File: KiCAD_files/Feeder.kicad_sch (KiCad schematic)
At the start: 82 parts, among them J405 Conn_01x02_Male, J406 Conn_01x02_Male, J501 Conn_01x03, Q501 60V N channel, Q502 TK13P25D,RQ, T501 PA2467NL, U407 OPA316, U501 NCP12700, U502 FODM217A, U503 TL431MFDT,215

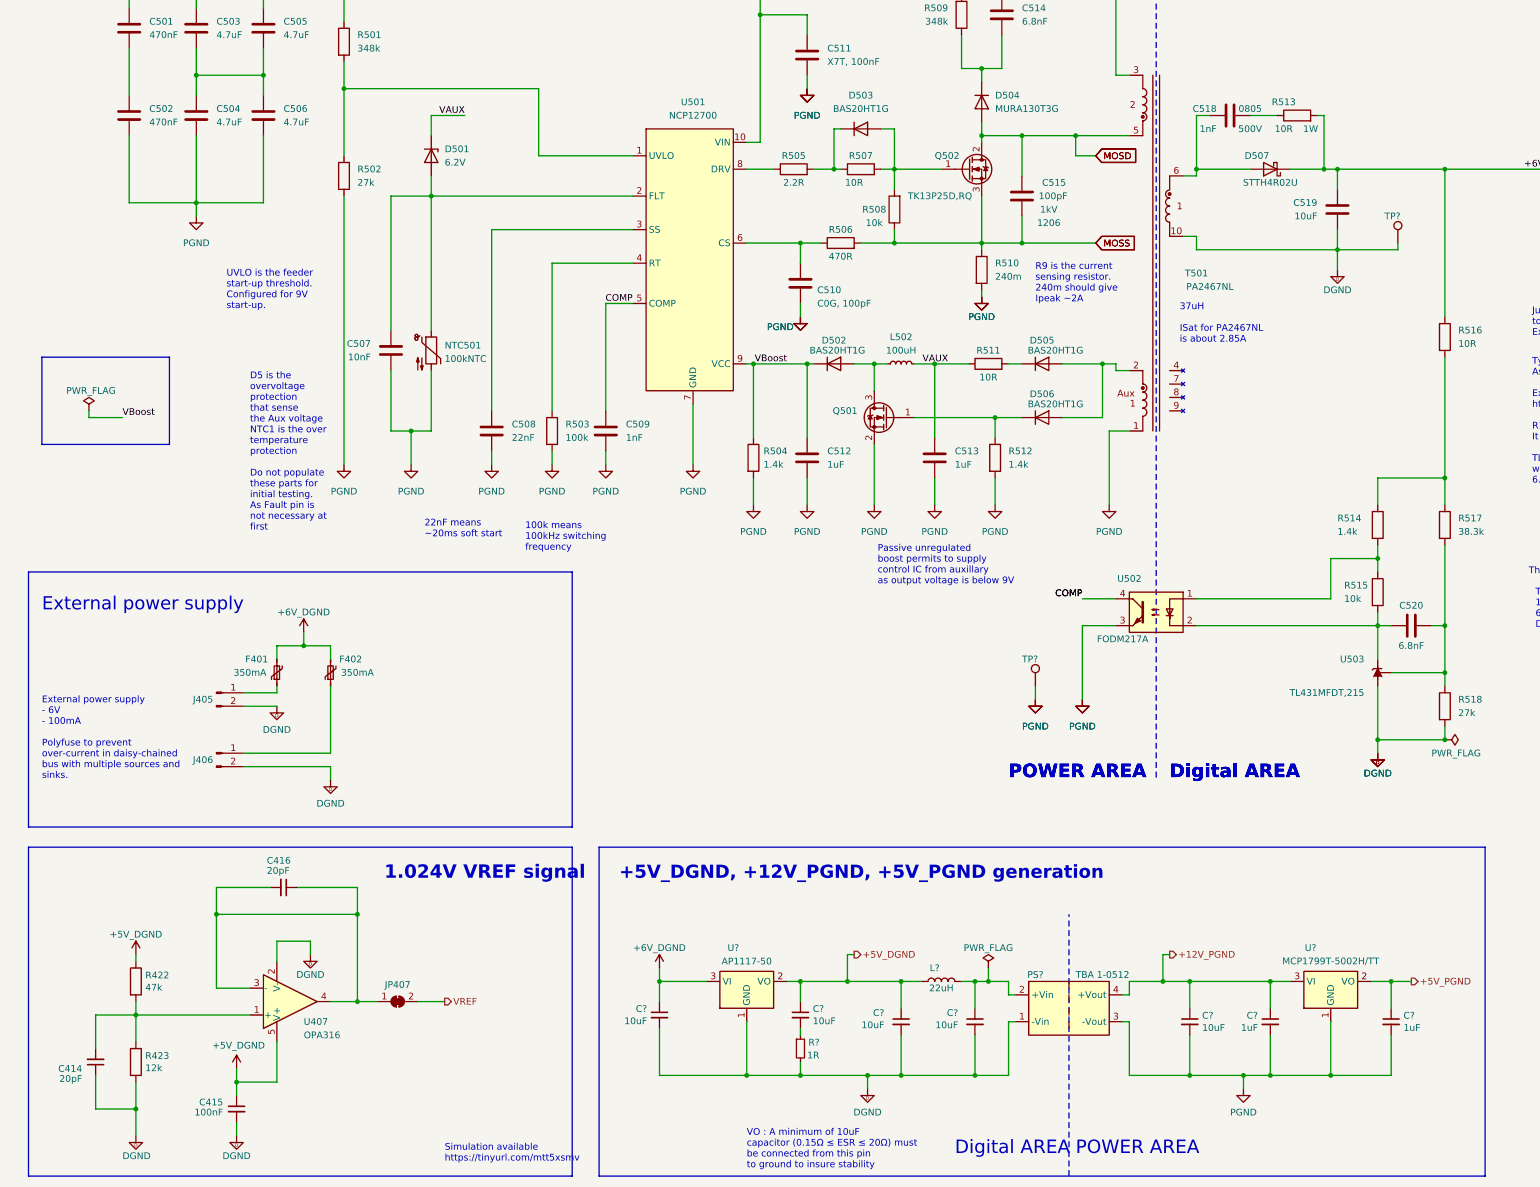
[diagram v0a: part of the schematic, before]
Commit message: Added ERC rules for galvanic isolation. Modified SPIN pinout.
Signed-off-by: Jean Alinei <jean.alinei@laas.fr>
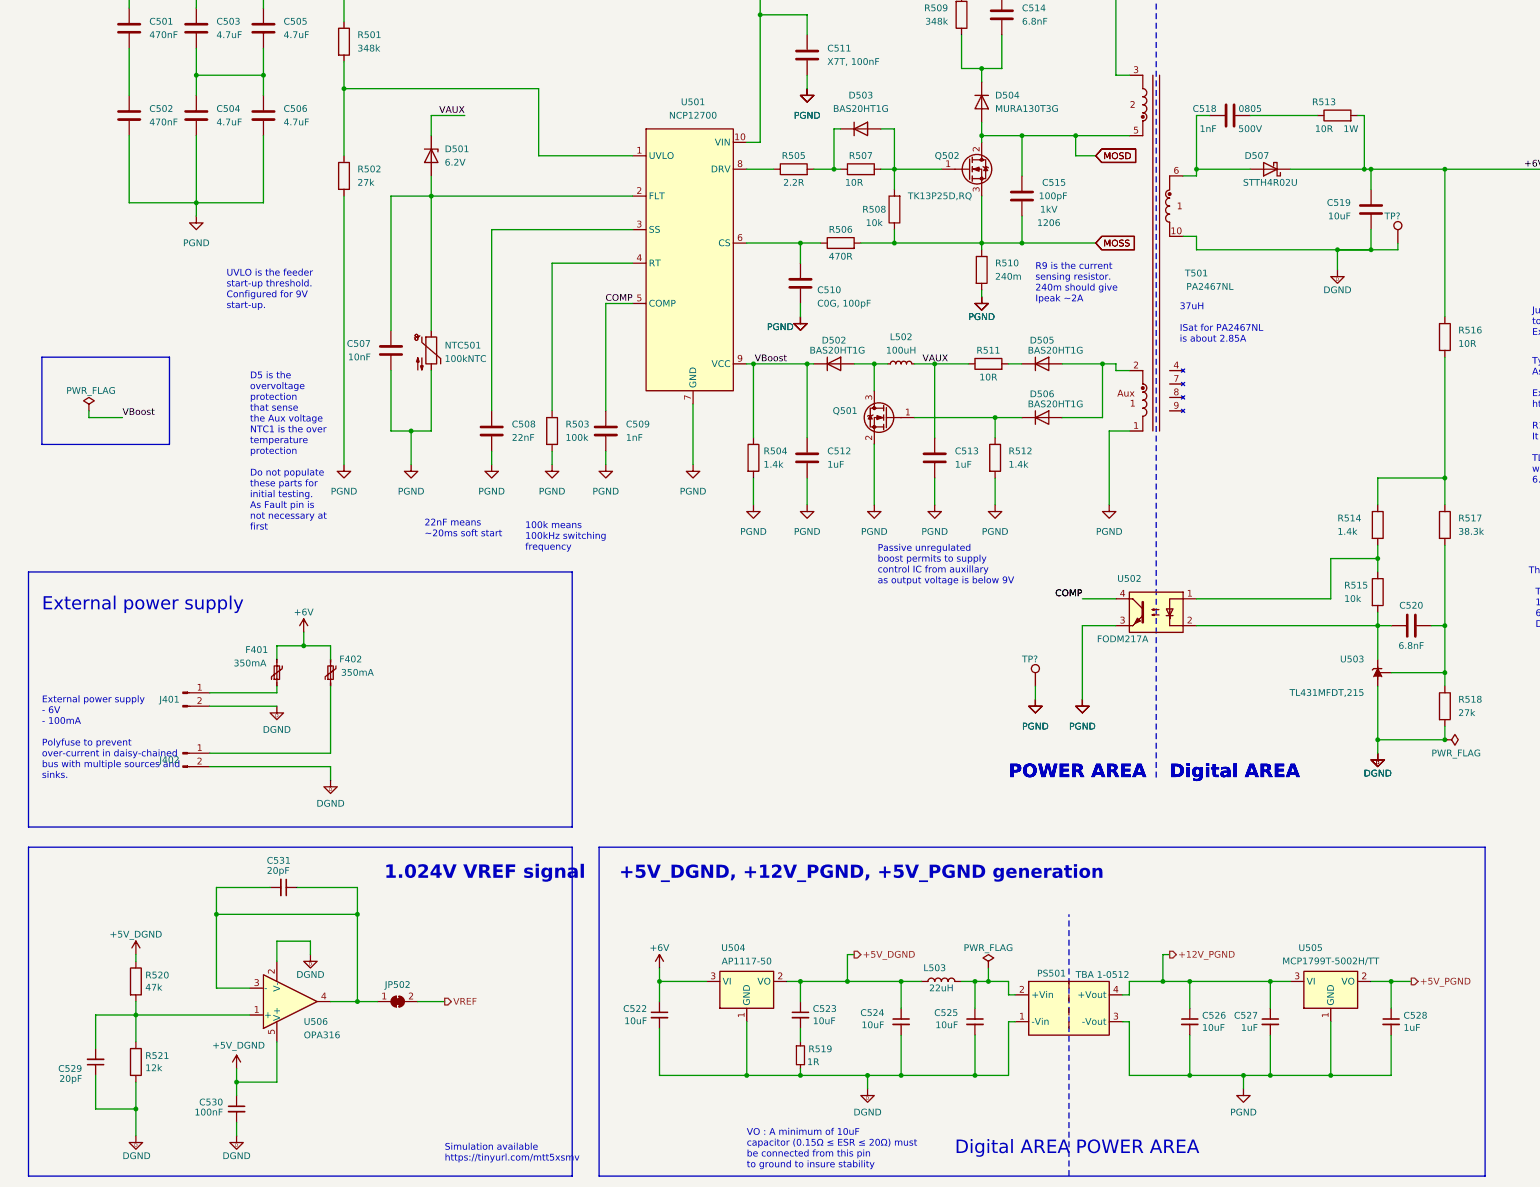
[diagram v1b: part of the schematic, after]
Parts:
- gave numbers to parts that had none: 12
- renumbered C414 to C529, C415 to C530, C416 to C531, J405 to J401, J406 to J402, JP407 to JP502, R422 to R520, R423 to R521, U407 to U506
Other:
- moved on the sheet: C519, J401, J402, R513, R519
